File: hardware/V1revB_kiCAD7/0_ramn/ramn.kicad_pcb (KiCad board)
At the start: 2 copper layers, 85.6 x 54 mm, 106 parts, among them J1 USB_C_Micro, J2 Screw_Terminal_01x03, J3 , J4 , J5 , J6 , U1 ATA6561-GAQW-N, U10 ATA6561-GAQW-N, U11 STM32L443CCTx, U12 NCV8163, U2 STM32L443CCTx, U3 NCV8163, U4 ATA6561-GAQW-N, U5 STM32L443CCTx, U6 NCV8163, U7 ATA6561-GAQW-N, U8 STM32L443CCTx, U9 NCV8163, Y1 NX3225GD-8MHZ-STD-CRA-3, Y2 NX3225GD-8MHZ-STD-CRA-3, Y3 NX3225GD-8MHZ-STD-CRA-3, Y4 NX3225GD-8MHZ-STD-CRA-3

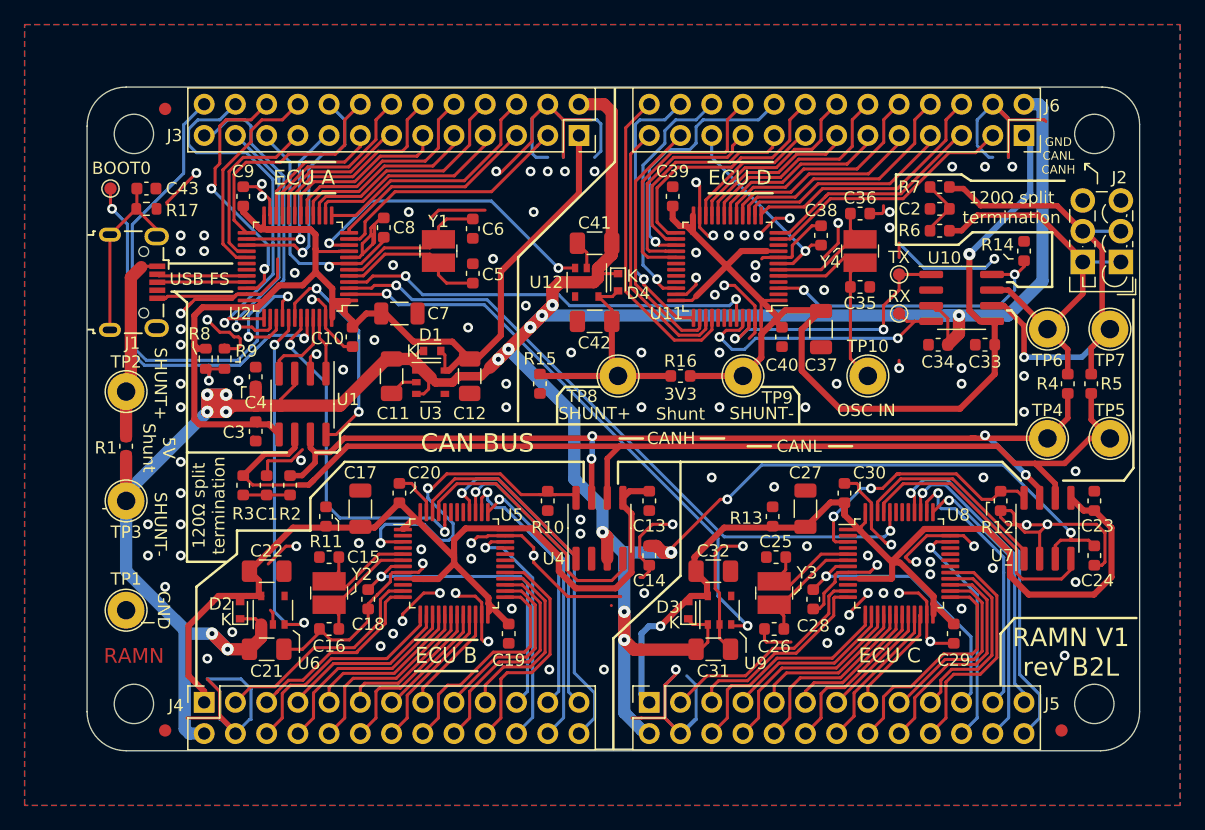
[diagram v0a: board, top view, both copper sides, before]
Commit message: Fixed board setup for DRC to match KiCAD 5 settings
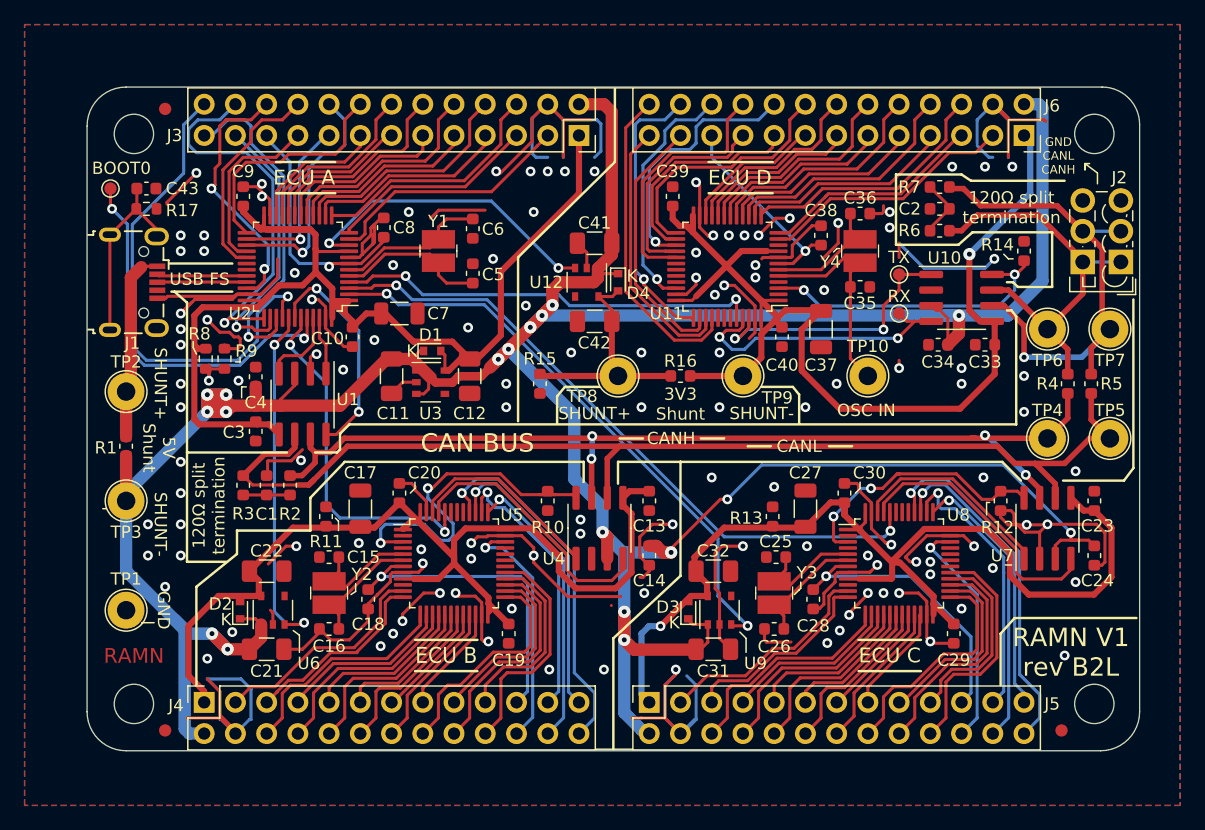
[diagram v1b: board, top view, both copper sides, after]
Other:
- net class 3V removed
- net class 5V removed
- net class CAN removed
- net class Default removed
